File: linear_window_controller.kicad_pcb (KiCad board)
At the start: 4 copper layers, 114.3 x 86.4 mm, 86 parts, among them J1 Motor 2, J2 Motor 1, J3 Motor 4, J4 Motor 3, J5 edge_psu_connector_64p, J9 Control, P1 ESP32 USB, SW2 Service, SW3 Service, SW4 Service, SW5 Service, SW6 Service, SW7 Service, U1 TSOP384xx, U10 TPS56220x, U2 DRV8874, U3 DRV8874, U4 DRV8874, U5 DRV8874, U6 PCF8574APWRG4, U8 ESP32-S3-WROOM-1-N16R2

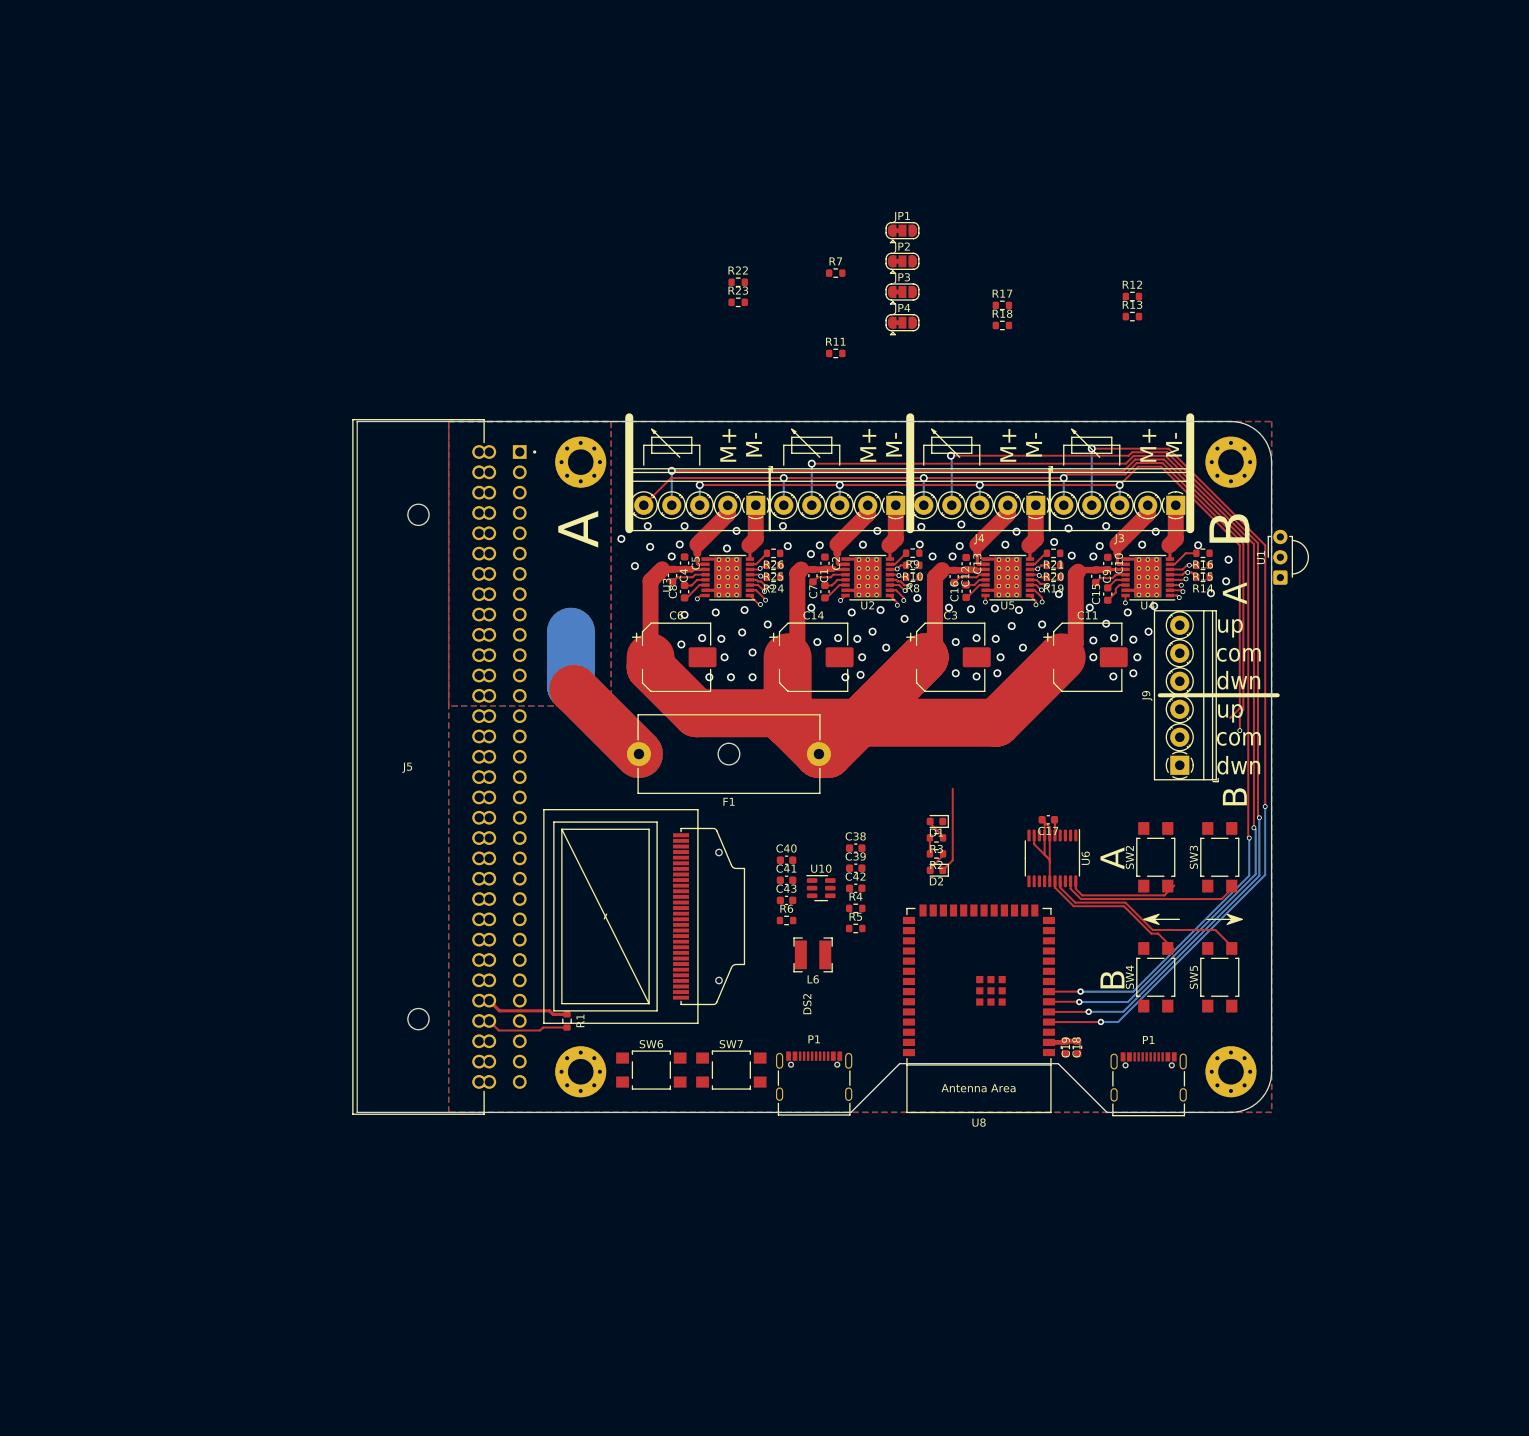
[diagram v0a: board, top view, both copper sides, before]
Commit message: Finish most of the routing, add DM9051 fast ethernet controller
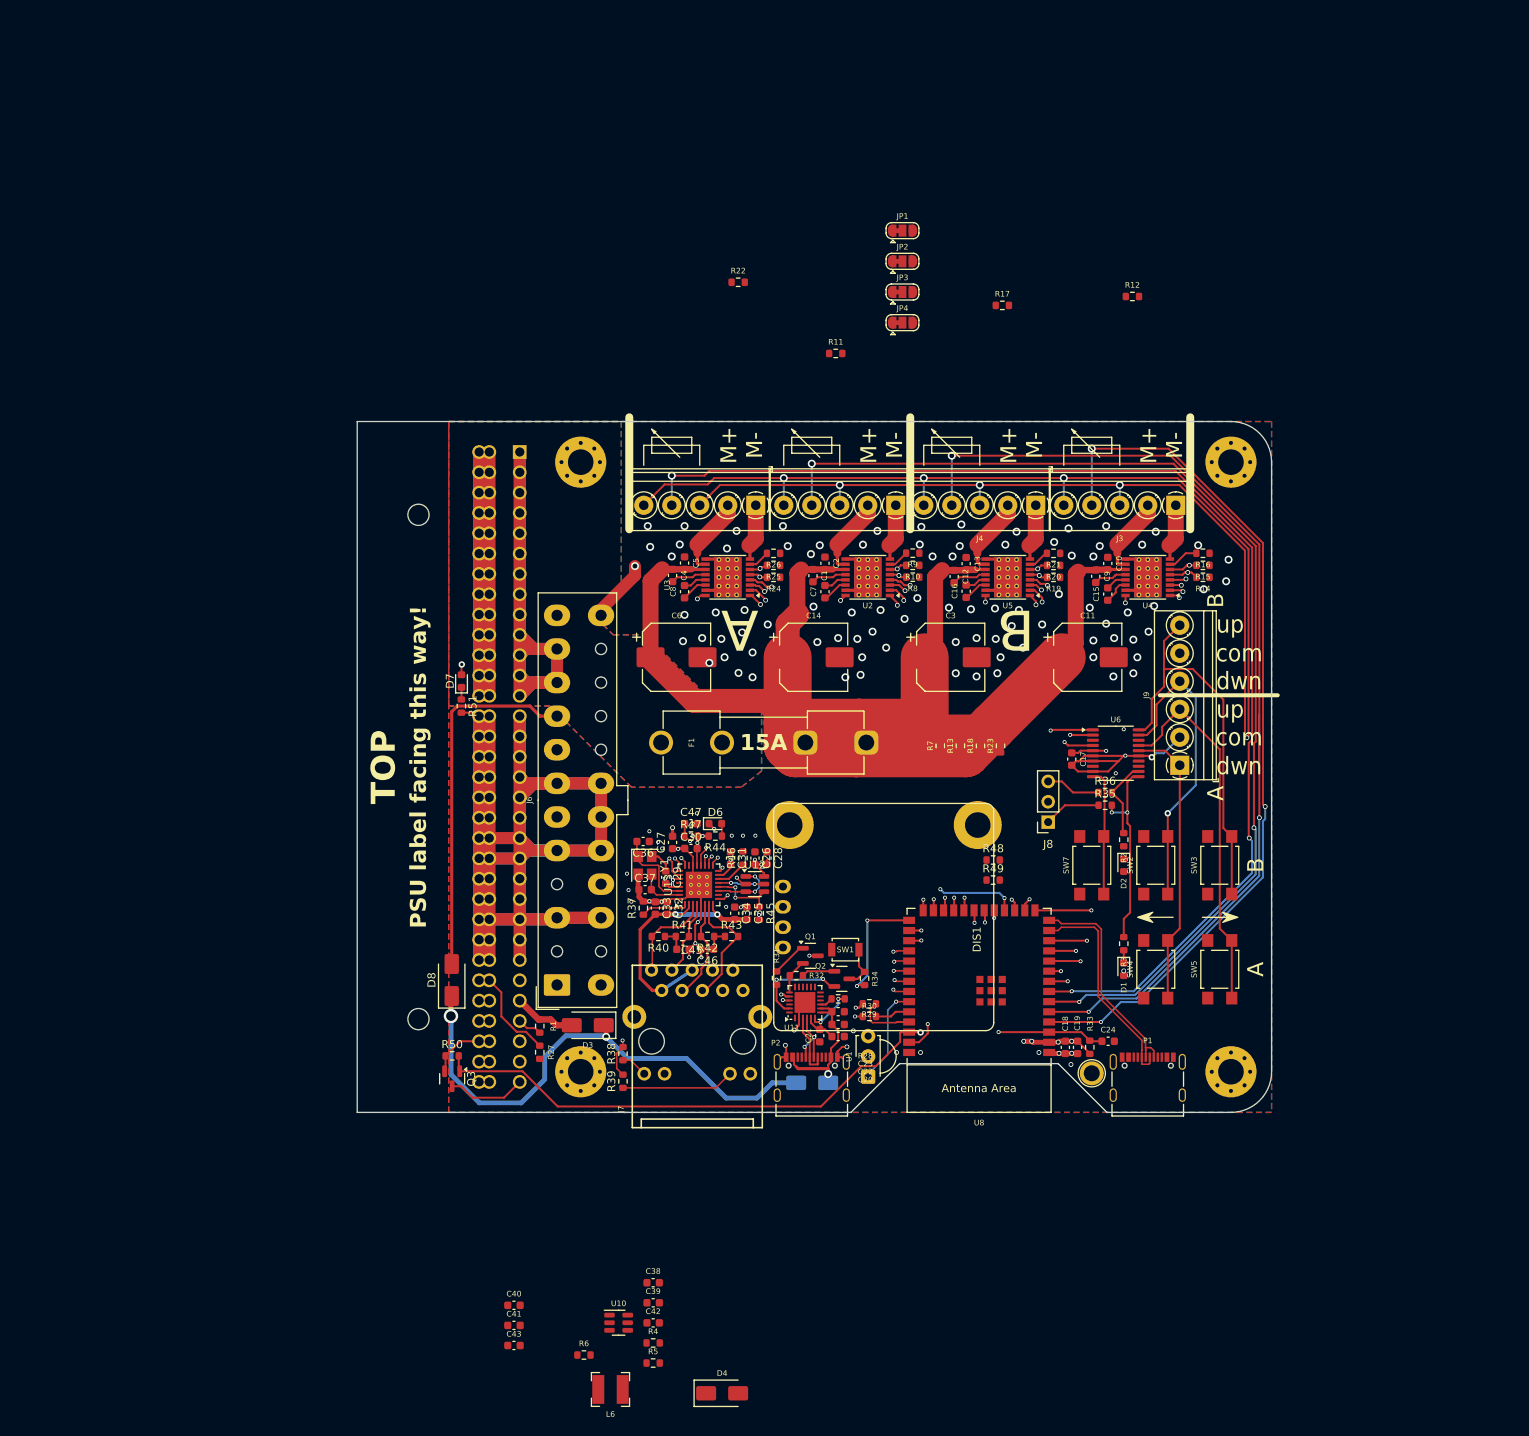
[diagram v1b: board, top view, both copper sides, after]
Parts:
- removed DS2: OLED-128O064D, iotta_footprints:OLED_0.96'_SSD1306_Folded
- removed the P1 at (100.3, 131.4)
- removed SW6: Service, Button_Switch_SMD:SW_SPST_TL3305B
- added C20: 22u, Capacitor_SMD:C_0603_1608Metric, F.Cu at (103.3, 126.4)
- added C21: 100n, Capacitor_SMD:C_0603_1608Metric, F.Cu at (101.0, 126.3)
- added C22: 22u, Capacitor_SMD:C_0603_1608Metric, F.Cu at (103.3, 124.9)
- added C23: 100n, Capacitor_SMD:C_0603_1608Metric, F.Cu at (103.3, 123.3)
- added C24: 100n, Capacitor_SMD:C_0603_1608Metric, F.Cu at (137.1, 127.0)
- added C26: 100n, Capacitor_SMD:C_0603_1608Metric, F.Cu at (92.9, 104.1)
- added C27: 22u, Capacitor_SMD:C_0603_1608Metric, F.Cu at (82.6, 102.2)
- added C28: 22u, Capacitor_SMD:C_0603_1608Metric, F.Cu at (94.4, 104.1)
- added C29: 100n, Capacitor_SMD:C_0603_1608Metric, F.Cu at (81.8, 106.5)
- added C30: 100n, Capacitor_SMD:C_0603_1608Metric, F.Cu at (84.9, 102.9)
- added C31: 100n, Capacitor_SMD:C_0603_1608Metric, F.Cu at (89.8, 104.1)
- added C32: 100n, Capacitor_SMD:C_0603_1608Metric, F.Cu at (82.0, 110.3)
- added C33: 22u, Capacitor_SMD:C_0603_1608Metric, F.Cu at (80.5, 110.3)
- added C34: 100n, Capacitor_SMD:C_0603_1608Metric, F.Cu at (90.4, 111.0)
- added C35: 22u, Capacitor_SMD:C_0603_1608Metric, F.Cu at (91.9, 111.0)
- added C36: 100n, Capacitor_SMD:C_0603_1608Metric, F.Cu at (78.9, 102.0)
- added C37: 100n, Capacitor_SMD:C_0603_1608Metric, F.Cu at (79.2, 108.0)
- added C45: 100n, Capacitor_SMD:C_0603_1608Metric, F.Cu at (83.9, 115.5)
- added C46: 100n, Capacitor_SMD:C_0603_1608Metric, F.Cu at (87.0, 115.5)
- added C47: 1u, Capacitor_SMD:C_0603_1608Metric, F.Cu at (84.9, 99.8)
- added D3: SS14, Diode_SMD:D_SMA, F.Cu at (72.0, 125.0)
- added D4: SS14, Diode_SMD:D_SMA, F.Cu at (88.8, 171.0)
- added D5: SS14, Diode_SMD:D_SMA, B.Cu at (100.1, 132.2)
- added D6: LED, LED_SMD:LED_0603_1608Metric, F.Cu at (88.0, 99.8)
- added D7: LED, LED_SMD:LED_0603_1608Metric, F.Cu at (56.2, 82.0)
- added D8: SS14, Diode_SMD:D_SMA, F.Cu at (55.0, 119.3)
- added DIS1: OLED_128x64, iotta_footprints:OLED_128x64_Module, F.Cu at (106.9, 111.5)
- added J6: ATX-24 (Molex 39-28-1243), Connector_Molex:Molex_Mini-Fit_Jr_5566-24A_2x12_P4.20mm_Vertical, F.Cu at (68.2, 120.0)
- added J7: Link-PP_LPJ0135GDNL, iotta_footprints:LinkPP_LPJ0135GDNL, F.Cu at (85.7, 127.0)
- added J8: EXT_LED, Connector_PinSocket_2.54mm:PinSocket_1x03_P2.54mm_Vertical, F.Cu at (129.6, 99.6)
- added P2: ESP32 USB, Connector_USB:USB_C_Receptacle_Palconn_UTC16-G, F.Cu at (100.0, 131.5)
- added Q1: BC817-40(SOT23), Package_TO_SOT_SMD:SOT-23, F.Cu at (99.8, 116.3)
- added Q2: BC817-40(SOT23), Package_TO_SOT_SMD:SOT-23, F.Cu at (103.8, 119.2)
- added Q3: BSS138, Package_TO_SOT_SMD:SOT-23, F.Cu at (55.1, 131.7)
- added R27: 0, Resistor_SMD:R_0603_1608Metric, F.Cu at (66.0, 128.4)
- added R28: 1k, Resistor_SMD:R_0603_1608Metric, F.Cu at (103.3, 121.7)
- added R29: 220, Resistor_SMD:R_0603_1608Metric, F.Cu at (107.2, 122.3)
- added R30: 220, Resistor_SMD:R_0603_1608Metric, F.Cu at (107.2, 123.9)
- added R31: 1k, Resistor_SMD:R_0603_1608Metric, F.Cu at (95.6, 119.1)
- added R32: 1k, Resistor_SMD:R_0603_1608Metric, F.Cu at (98.1, 118.8)
- added R33: 10k, Resistor_SMD:R_0603_1608Metric, F.Cu at (134.8, 127.8)
- added R34: 100, Resistor_SMD:R_0603_1608Metric, F.Cu at (106.6, 119.2)
- added R35: 100, Resistor_SMD:R_0603_1608Metric, F.Cu at (136.7, 97.5)
- added R36: 100, Resistor_SMD:R_0603_1608Metric, F.Cu at (136.7, 95.9)
- added R37: 6k8, Resistor_SMD:R_0603_1608Metric, F.Cu at (79.0, 110.3)
- added R38: 300, Resistor_SMD:R_0603_1608Metric, F.Cu at (76.4, 128.6)
- added R39: 300, Resistor_SMD:R_0603_1608Metric, F.Cu at (76.4, 132.0)
- added R40: 49.9, Resistor_SMD:R_0603_1608Metric, F.Cu at (80.8, 113.9)
- added R41: 49.9, Resistor_SMD:R_0603_1608Metric, F.Cu at (83.8, 113.9)
- added R42: 49.9, Resistor_SMD:R_0603_1608Metric, F.Cu at (87.0, 113.9)
- added R43: 49.9, Resistor_SMD:R_0603_1608Metric, F.Cu at (90.0, 113.9)
- added R44: 300, Resistor_SMD:R_0603_1608Metric, F.Cu at (88.0, 101.3)
- added R45: 10k, Resistor_SMD:R_0603_1608Metric, F.Cu at (93.4, 111.0)
- added R46: 10k, Resistor_SMD:R_0603_1608Metric, F.Cu at (91.4, 104.1)
- added R47: 10k, Resistor_SMD:R_0603_1608Metric, F.Cu at (84.9, 101.3)
- added R48: 10k, Resistor_SMD:R_0603_1608Metric, F.Cu at (122.7, 104.3)
- added R49: 10k, Resistor_SMD:R_0603_1608Metric, F.Cu at (122.7, 106.8)
- added R50: 10k, Resistor_SMD:R_0603_1608Metric, F.Cu at (55.1, 128.8)
- added R51: 300, Resistor_SMD:R_0603_1608Metric, F.Cu at (56.2, 85.1)
- added REF**: TestPoint_Plated_Hole_D2.0mm, TestPoint:TestPoint_Plated_Hole_D2.0mm, F.Cu at (135.0, 131.0)
- added SW1: PGM, Button_Switch_SMD:SW_SPST_B3U-1000P, F.Cu at (104.2, 115.5)
- added U11: CP2102N-A01-GQFN24, Package_DFN_QFN:QFN-24-1EP_4x4mm_P0.5mm_EP2.6x2.6mm, F.Cu at (99.2, 122.2)
- added U12: 93LCxxAxxOT, Package_TO_SOT_SMD:SOT-23-6, F.Cu at (92.9, 107.3)
- added U13: DM9051, Package_DFN_QFN:QFN-32-1EP_5x5mm_P0.5mm_EP3.3x3.3mm_ThermalVias, F.Cu at (85.9, 107.5)
- added Y1: 25MHz YXC X322525MOB4SI, Crystal:Crystal_SMD_3225-4Pin_3.2x2.5mm, F.Cu at (79.1, 105.0)
- F1: footprint Fuse:Fuseholder_Cylinder-5x20mm_Schurter_0031_8201_Horizontal_Open -> Fuse:Fuseholder_Clip-6.3x32mm_Littelfuse_102_122_Inline_P34.21x7.62mm_D1.98mm_Horizontal
- J5: value edge_psu_connector_64p -> Amphenol 10053363-200LF; footprint iotta_footprints_v6:Amphenol_10053363-200LF_WingTAT ER64BGFBK_Compatible -> iotta_footprints_v6:Amphenol_10053363-200LF_WingTAT ER64BGFBK_Compatible_BOTTOM
- moved U1 80.9 mm to (107.0, 131.4)
- moved C43 65.2 mm to (62.8, 165.0)
- moved C40 65.2 mm to (62.8, 160.0)
- moved C41 65.2 mm to (62.8, 162.5)
- moved R23 64.4 mm to (123.6, 90.1), turned to 90 degrees
- moved R7 60.5 mm to (116.1, 90.1), turned to 90 degrees
- moved C38 59.9 mm to (80.2, 157.2)
- moved R4 59.9 mm to (80.2, 164.7)
- moved U10 59.9 mm to (75.9, 162.2)
- moved C39 59.9 mm to (80.2, 159.7)
- moved C42 59.9 mm to (80.2, 162.2)
- moved L6 59.9 mm to (74.8, 170.5)
- moved R5 59.9 mm to (80.2, 167.2)
- moved R6 59.9 mm to (71.5, 166.2)
- moved R13 57.8 mm to (118.6, 90.1), turned to 90 degrees
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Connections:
- C40 pad 2: +12P -> /DCDC_IN
- C41 pad 2: +12P -> /DCDC_IN
- C43 pad 2: +12P -> /DCDC_IN
- D1 pad 1: /LED_F1 -> Net-(D1-K)
- D1 pad 2: Net-(D1-A) -> +3.3V
- D2 pad 1: /LED_F2 -> Net-(D2-K)
- D2 pad 2: Net-(D2-A) -> +3.3V
- J5 pad A27: GND -> Net-(J5-ADDR)
- J5 pad B28: +12P -> +V12SB
- P1 pad A1: Net-(P1-GND-PadA1) -> GND
- P1 pad A12: Net-(P1-GND-PadA1) -> GND
- P1 pad A6: unconnected-(P1-D+-PadA6) -> /ESPUSB+
- P1 pad A7: unconnected-(P1-D--PadA7) -> /ESPUSB-
- P1 pad B1: Net-(P1-GND-PadA1) -> GND
- P1 pad B12: Net-(P1-GND-PadA1) -> GND
- P1 pad B6: (no net) -> /ESPUSB+
- P1 pad B7: (no net) -> /ESPUSB-
- P1 pad S1: unconnected-(P1-SHIELD-PadS1) -> GND
- R1 pad 2: +12P -> +V12SB
- R2 pad 1: Net-(D2-A) -> /LED_F2
- R2 pad 2: +3.3V -> Net-(D2-K)
- R3 pad 1: Net-(D1-A) -> /LED_F1
- R3 pad 2: +3.3V -> Net-(D1-K)
- R6 pad 1: +12P -> /DCDC_IN
- SW2 pad 2: /A_UP -> /B_UP
- SW3 pad 2: /A_DWN -> /B_DWN
- SW4 pad 2: /B_UP -> /A_UP
- SW5 pad 2: /B_DWN -> /A_DWN
- U1 pad 1: unconnected-(U1-OUT-Pad1) -> /IR_REMOTE
- U1 pad 2: unconnected-(U1-GND-Pad2) -> GND
- U1 pad 3: unconnected-(U1-Vs-Pad3) -> +3.3V
- U10 pad 1: +12P -> /DCDC_IN
- U6 pad 1: unconnected-(U6-~{INT}-Pad1) -> /~{IOEX1_INT}
- U6 pad 10: /LED_F1 -> /BTN_FUNC
- U6 pad 11: /LED_F2 -> /LED_F1
- U6 pad 12: /BTN_FUNC -> /LED_F2
- U6 pad 16: /B_UP -> /A_UP
- U6 pad 17: /B_DWN -> /A_DWN
- U6 pad 19: /A_DWN -> /B_UP
- U6 pad 20: /A_UP -> /B_DWN
- U8 pad 1: Net-(U8-GND-Pad1) -> GND
- U8 pad 10: unconnected-(U8-GPIO17/U1TXD/ADC2_CH6-Pad10) -> /DRV4_IN1
- U8 pad 11: unconnected-(U8-GPIO18/U1RXD/ADC2_CH7/CLK_OUT3-Pad11) -> /DRV4_IN2
- U8 pad 12: unconnected-(U8-GPIO8/TOUCH8/ADC1_CH7/SUBSPICS1-Pad12) -> /~{DRV4_FAULT}
- U8 pad 13: unconnected-(U8-GPIO19/U1RTS/ADC2_CH8/CLK_OUT2/USB_D--Pad13) -> /ESPUSB-
- U8 pad 14: unconnected-(U8-GPIO20/U1CTS/ADC2_CH9/CLK_OUT1/USB_D+-Pad14) -> /ESPUSB+
- U8 pad 15: unconnected-(U8-GPIO3/TOUCH3/ADC1_CH2-Pad15) -> /DRV4_IPROPI
- U8 pad 16: unconnected-(U8-GPIO46-Pad16) -> /~{IOEX1_INT}
- U8 pad 17: unconnected-(U8-GPIO9/TOUCH9/ADC1_CH8/FSPIHD/SUBSPIHD-Pad17) -> /DRV3_IPROPI
- U8 pad 18: unconnected-(U8-GPIO10/TOUCH10/ADC1_CH9/FSPICS0/FSPIIO4/SUBSPICS0-Pad18) -> /DRV2_IPROPI
- U8 pad 19: unconnected-(U8-GPIO11/TOUCH11/ADC2_CH0/FSPID/FSPIIO5/SUBSPID-Pad19) -> /DRV3_IN1
- U8 pad 20: unconnected-(U8-GPIO12/TOUCH12/ADC2_CH1/FSPICLK/FSPIIO6/SUBSPICLK-Pad20) -> /DRV3_IN2
- U8 pad 21: unconnected-(U8-GPIO13/TOUCH13/ADC2_CH2/FSPIQ/FSPIIO7/SUBSPIQ-Pad21) -> /~{DRV3_FAULT}
- U8 pad 22: unconnected-(U8-GPIO14/TOUCH14/ADC2_CH3/FSPIWP/FSPIDQS/SUBSPIWP-Pad22) -> /~{DRV2_FAULT}
- U8 pad 23: unconnected-(U8-GPIO21-Pad23) -> /DRV2_IN2
- U8 pad 24: unconnected-(U8-GPIO47/SPICLK_P/SUBSPICLK_P_DIFF-Pad24) -> /DRV2_IN1
- U8 pad 25: unconnected-(U8-GPIO48/SPICLK_N/SUBSPICLK_N_DIFF-Pad25) -> /~{DRV1_FAULT}
- U8 pad 26: unconnected-(U8-GPIO45-Pad26) -> /~{DRV_SLEEP}
- U8 pad 27: unconnected-(U8-GPIO0/BOOT-Pad27) -> /~{ESP_PGM}
- U8 pad 28: unconnected-(U8-SPIIO6/GPIO35/FSPID/SUBSPID-Pad28) -> /DRV1_IN2
- U8 pad 29: unconnected-(U8-SPIIO7/GPIO36/FSPICLK/SUBSPICLK-Pad29) -> /DRV1_IN1
- U8 pad 3: unconnected-(U8-EN-Pad3) -> /ESP_EN
- U8 pad 30: unconnected-(U8-SPIDQS/GPIO37/FSPIQ/SUBSPIQ-Pad30) -> /LAN_MISO
- U8 pad 31: unconnected-(U8-GPIO38/FSPIWP/SUBSPIWP-Pad31) -> /LAN_MOSI
- U8 pad 32: unconnected-(U8-MTCK/GPIO39/CLK_OUT3/SUBSPICS1-Pad32) -> /LAN_CK
- U8 pad 33: unconnected-(U8-MTDO/GPIO40/CLK_OUT2-Pad33) -> /LAN_CSN
- U8 pad 34: unconnected-(U8-MTDI/GPIO41/CLK_OUT1-Pad34) -> /~{LAN_INT}
- U8 pad 35: unconnected-(U8-MTMS/GPIO42-Pad35) -> /IR_REMOTE
- U8 pad 36: unconnected-(U8-U0RXD/GPIO44/CLK_OUT2-Pad36) -> /U0RXD
- U8 pad 37: unconnected-(U8-U0TXD/GPIO43/CLK_OUT1-Pad37) -> /U0TXD
- U8 pad 38: unconnected-(U8-GPIO2/TOUCH2/ADC1_CH1-Pad38) -> /PS_ENABLE
- U8 pad 39: unconnected-(U8-GPIO1/TOUCH1/ADC1_CH0-Pad39) -> /DRV1_IPROPI
- U8 pad 40: Net-(U8-GND-Pad1) -> GND
- U8 pad 41: Net-(U8-GND-Pad1) -> GND
- U8 pad 8: unconnected-(U8-GPIO15/U0RTS/ADC2_CH4/XTAL_32K_P-Pad8) -> /SCL
- U8 pad 9: unconnected-(U8-GPIO16/U0CTS/ADC2_CH5/XTAL_32K_N-Pad9) -> /SDA
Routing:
- net GND: track 38.4 -> 432.9 mm, vias 88 -> 122
- net /+12V_UNFUSED: track 30.4 -> 232.8 mm
- net /PS_ENABLE: track 0.00 -> 65.9 mm, vias 0 -> 1
- net /DCDC_IN: track 0.00 -> 65.2 mm, vias 0 -> 2
- net /PS_OK: track 0.00 -> 63.0 mm, vias 0 -> 1
- net +3.3V: track 7.59 -> 61.8 mm, vias 0 -> 17
- net /DRV1_IPROPI: track 21.6 -> 73.0 mm, vias 1 -> 2
- net /LAN_SPEED: track 0.00 -> 47.1 mm, vias 0 -> 1
- net +5VSB: track 0.00 -> 45.5 mm
- net /ESP_EN: track 0.00 -> 42.1 mm, vias 0 -> 2
- net /PS_ON: track 0.00 -> 38.8 mm
- net /~{LAN_INT}: track 0.00 -> 38.0 mm, vias 0 -> 2
- net /~{DRV3_FAULT}: track 17.0 -> 53.9 mm, vias 1 -> 2
- net /SCL: track 0.00 -> 36.8 mm, vias 0 -> 2
- net /DRV4_IN2: track 20.5 -> 55.9 mm, vias 1 -> 2
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- added copper zone on In1.Cu, net +3.3V
- added copper zone on In2.Cu, net GND
- removed copper zone on In1.Cu, net GND
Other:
- board text added: "15A"
- board text added: "PSU label facing this way!"
- board text added: "TOP"
